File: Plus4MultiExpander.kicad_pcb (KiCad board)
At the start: 2 copper layers, 62.2 x 99.9 mm, 11 parts, among them CN1 EDGE_CONN, CN2 C16_NEWSTYLE_EXP_PORT_1, CN3 C16_NEWSTYLE_EXP_PORT_2, CN4 C16_NEWSTYLE_EXP_PORT_3, U1 74LS245, U2 74LS245

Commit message: More honing
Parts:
- moved D1 0.25 mm to (136.5, 134.5)
- moved D2 0.25 mm to (140.8, 134.5)
- moved R1 0.25 mm to (132.2, 134.5)

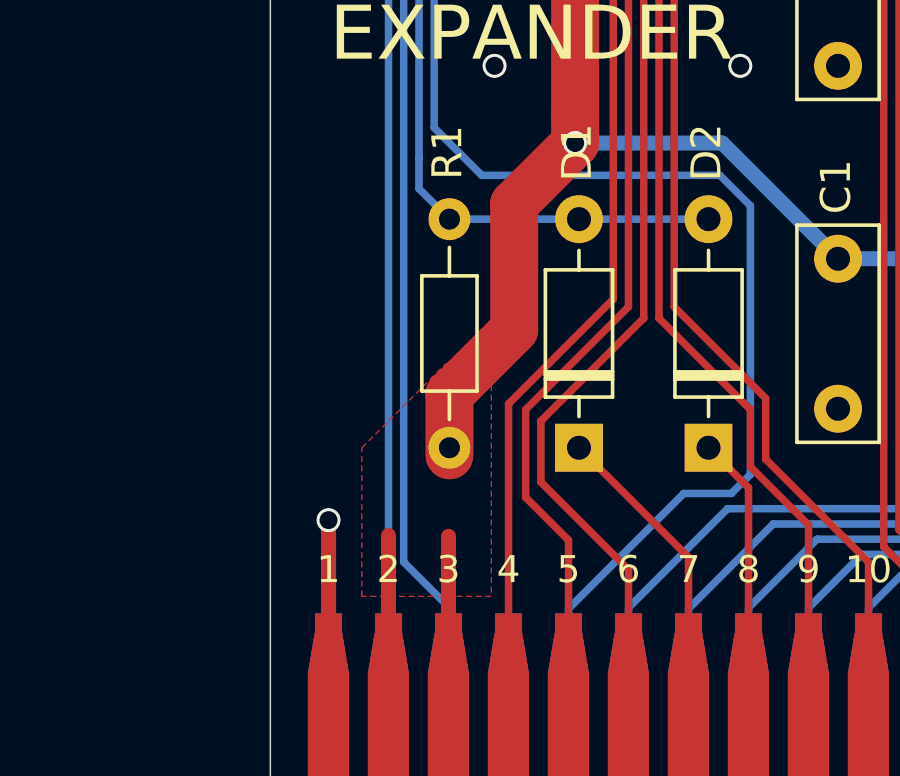
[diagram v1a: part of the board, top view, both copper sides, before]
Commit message: Add 3D model of connector
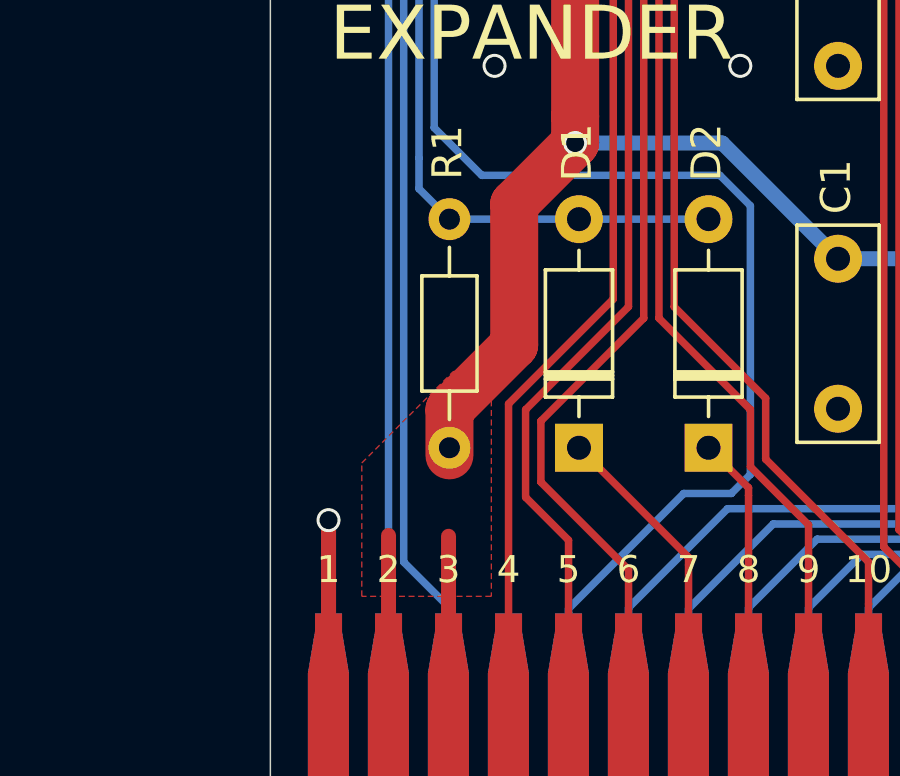
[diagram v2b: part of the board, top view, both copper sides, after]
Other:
- board text added: "INSPIRED BY WORK FROM SOLDER/SYNERGY"

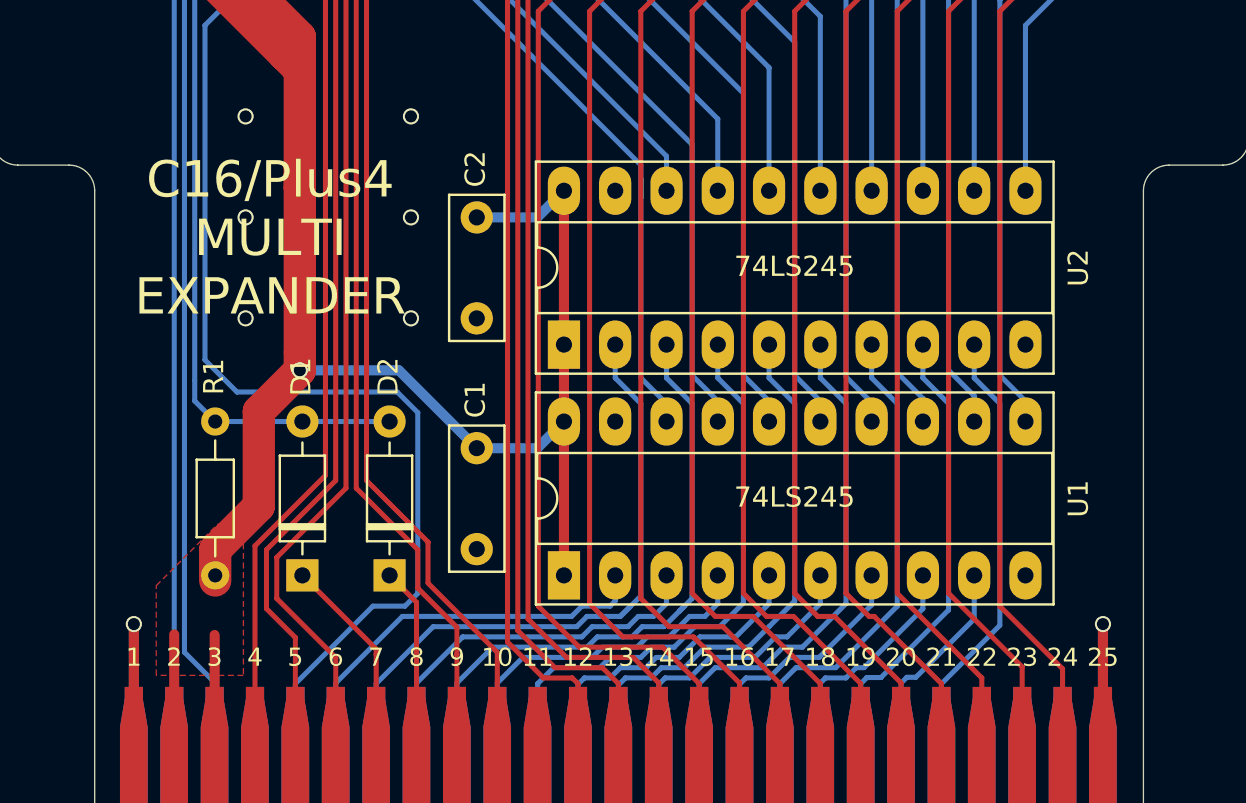
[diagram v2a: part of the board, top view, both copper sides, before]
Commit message: Tidy up silkscreen
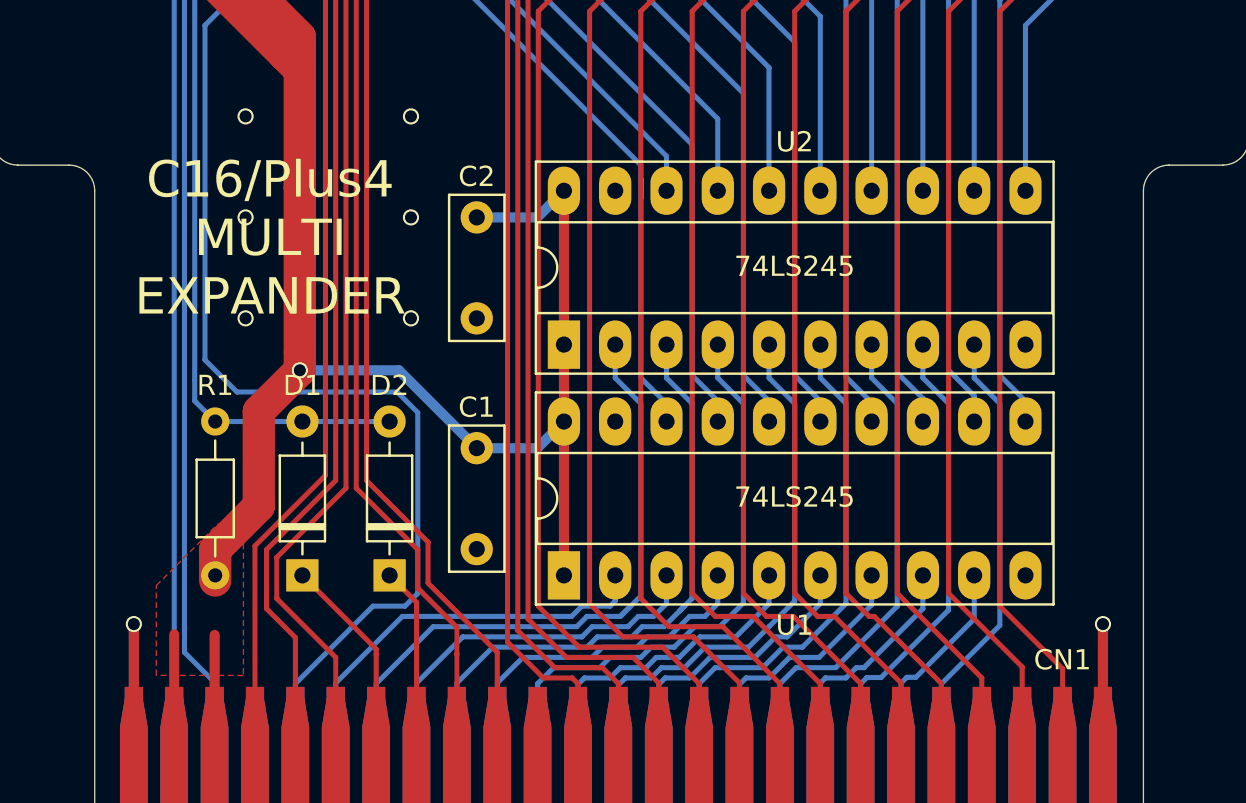
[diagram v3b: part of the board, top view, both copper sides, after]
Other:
- board text removed: "1"
- board text removed: "10"
- board text removed: "11"
- board text removed: "12"
- board text removed: "13"
- board text removed: "14"
- board text removed: "15"
- board text removed: "16"
- board text removed: "17"
- board text removed: "18"
- board text removed: "19"
- board text removed: "2"
- board text removed: "20"
- board text removed: "21"
- board text removed: "22"
- board text removed: "23"
- board text removed: "24"
- board text removed: "25"
- board text removed: "3"
- board text removed: "4"
- board text removed: "5"
- board text removed: "6"
- board text removed: "7"
- board text removed: "8"
- board text removed: "9"
- board text removed: "A"
- board text removed: "AA"
- board text removed: "B"
- board text removed: "BB"
- board text removed: "C"
- board text removed: "CC"
- board text removed: "D"
- board text removed: "E"
- board text removed: "F"
- board text removed: "H"
- board text removed: "J"
- board text removed: "K"
- board text removed: "L"
- board text removed: "M"
- board text removed: "N"
- board text removed: "P"
- board text removed: "R"
- board text removed: "S"
- board text removed: "T"
- board text removed: "U"
- board text removed: "V"
- board text removed: "W"
- board text removed: "X"
- board text removed: "Y"
- board text removed: "Z"

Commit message: Add credits and license
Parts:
- added C3: 220u, Capacitor_THT:CP_Radial_D8.0mm_P3.50mm, F.Cu at (128.1, 85.9)
- added V0: LICENSE, Plus4MultiExpander:cc_by_nc_sa, B.Cu at (135.9, 119.3)
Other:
- board text added: "CC-BY-NC-SA © SukkoPera 2023 Inspired by work from Solder/Synergy github.com/SukkoPera/Plus4MultiExpander"
- board text removed: "INSPIRED BY WORK FROM SOLDER/SYNERGY"

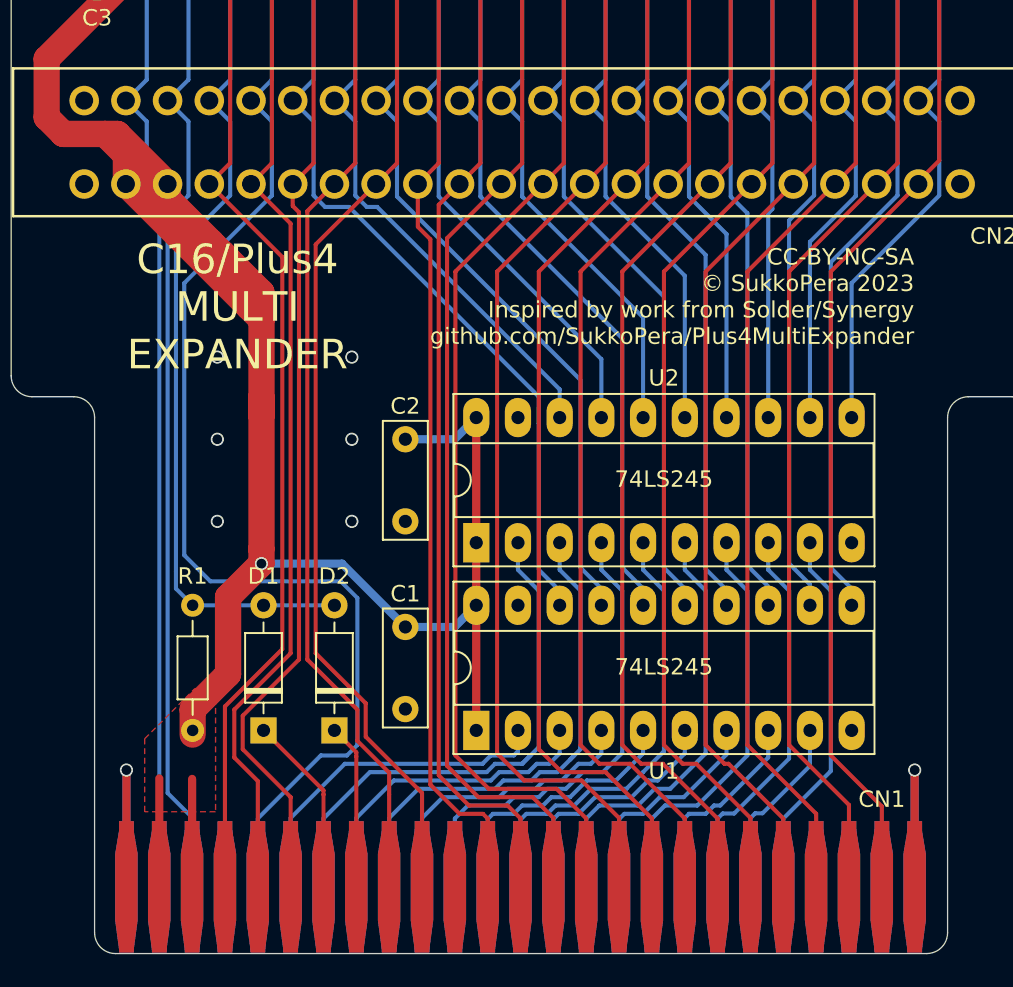
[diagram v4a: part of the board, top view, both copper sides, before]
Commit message: Generate /C2 with NAND gate
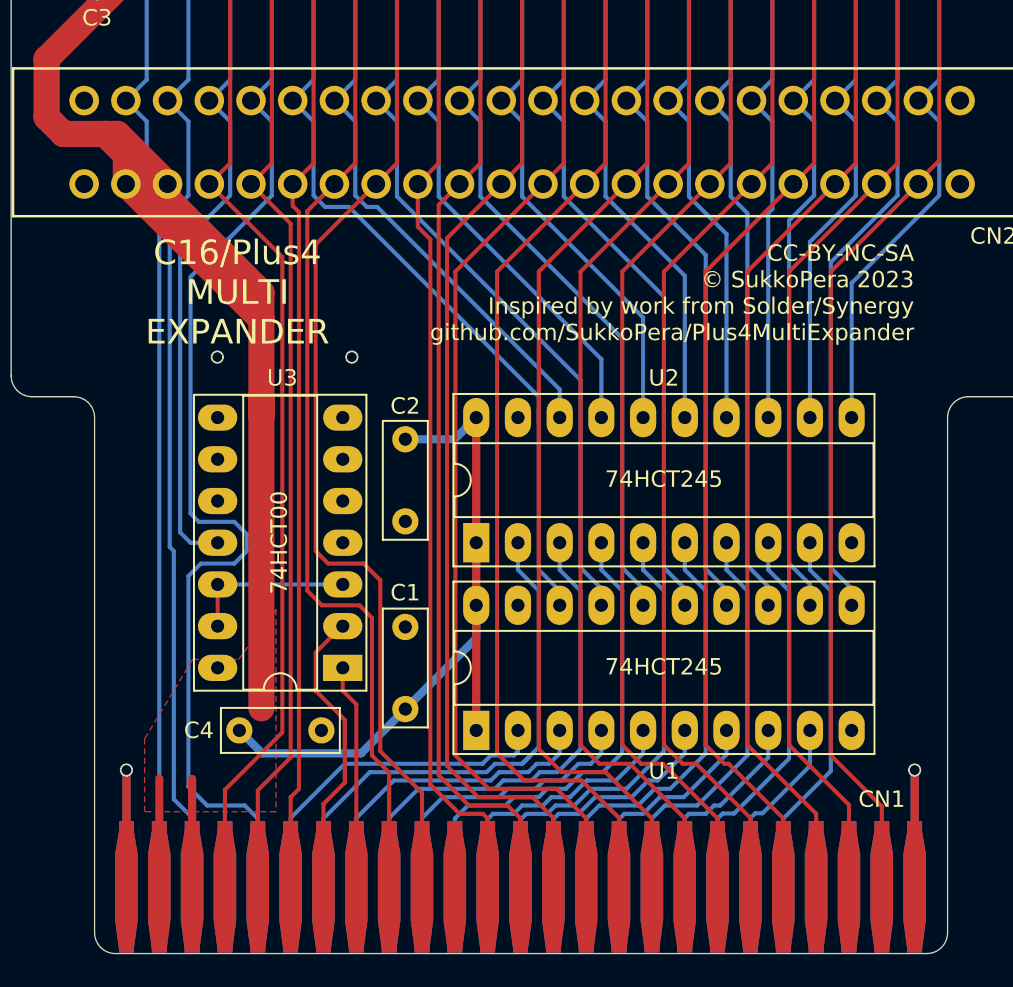
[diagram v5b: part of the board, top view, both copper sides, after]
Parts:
- removed D1, D2: 1n4148, Diode_THT:D_DO-35_SOD27_P7.62mm_Horizontal
- removed R1: 4.7k, Resistor_THT:R_Axial_DIN0204_L3.6mm_D1.6mm_P7.62mm_Horizontal
- added C4: 100n, Capacitor_THT:C_Disc_D7.0mm_W2.5mm_P5.00mm, F.Cu at (135.1, 134.5)
- added U3: 74HCT00, Package_DIP:DIP-14_W7.62mm_Socket_LongPads, F.Cu at (141.4, 130.7)
- U1, U2: value 74LS245 -> 74HCT245
- moved V0 19.1 mm to (152.3, 109.5)
- moved C1 5.00 mm to (145.2, 133.2), turned to 90 degrees
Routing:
- net /~c2: track 89.8 -> 78.7 mm
- net Net-(U3-Pad12): track 0.00 -> 10.2 mm
- net /~c2lo: track 11.0 -> 17.9 mm
- net /phi0: track 115.2 -> 111.0 mm
- net /~c2hi: track 10.1 -> 13.9 mm
- net /~c1hi: track 93.7 -> 91.2 mm
- net +5V: track 241.0 -> 242.4 mm, vias 1 -> 0
- net /~cs1: track 93.6 -> 95.0 mm
- net /~cs0: track 95.1 -> 96.4 mm
- net /r_~w: track 93.9 -> 92.7 mm
- net GND: vias 8 -> 4

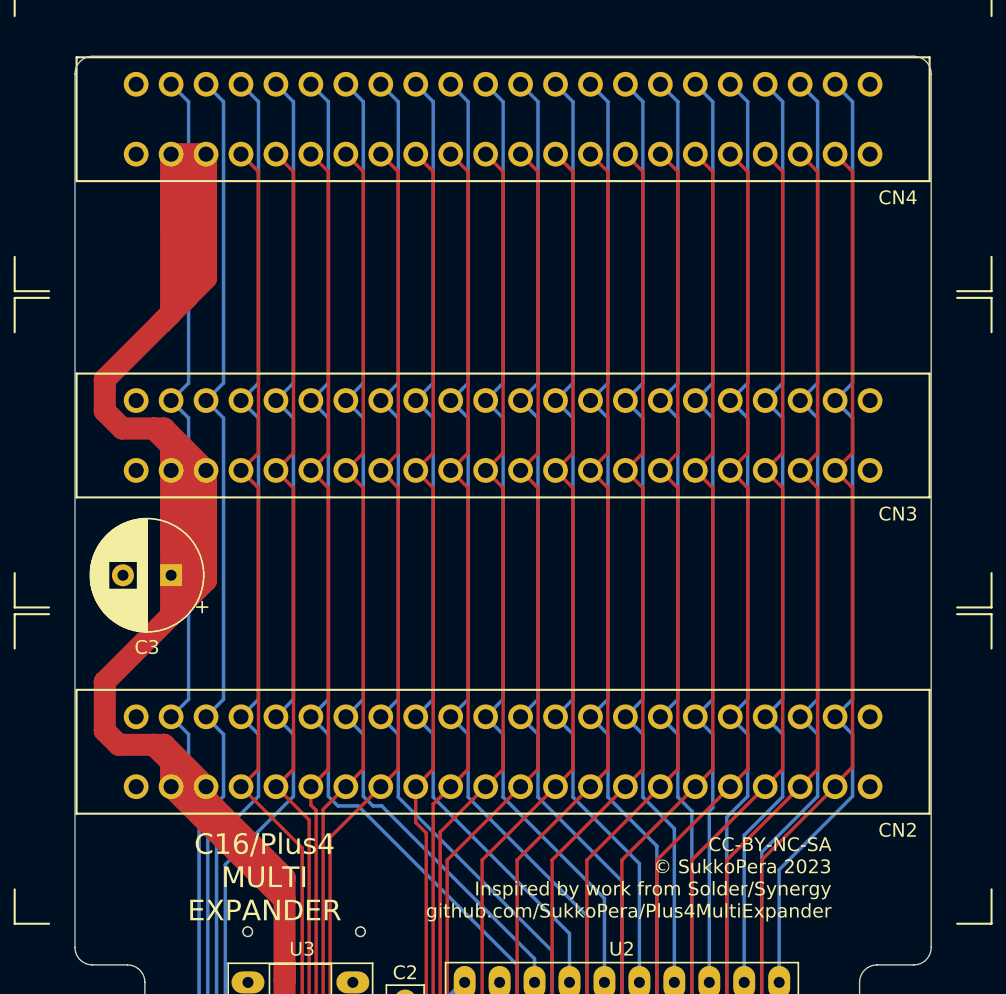
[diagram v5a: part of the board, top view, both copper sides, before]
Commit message: Add standoff holes
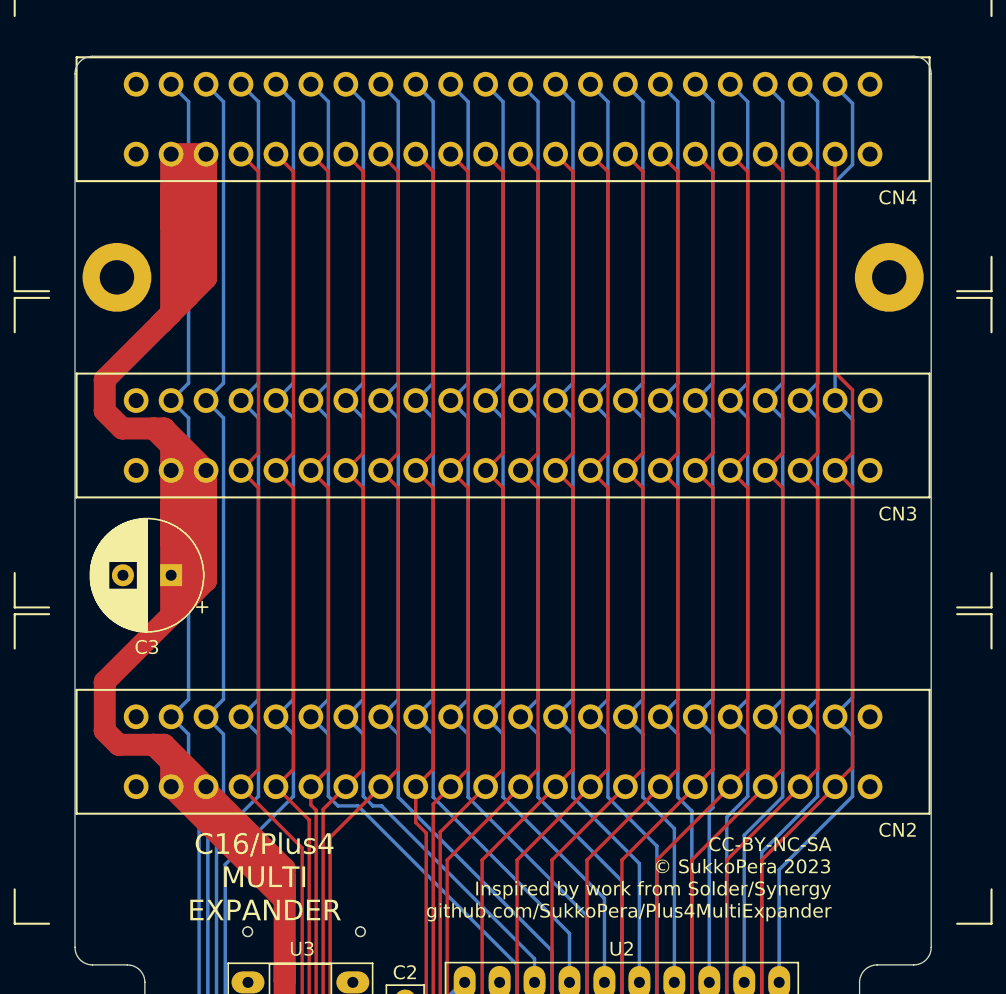
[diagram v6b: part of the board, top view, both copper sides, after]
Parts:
- added H1: HOLE_STANDOFF, MountingHole:MountingHole_2.5mm_Pad, F.Cu at (124.2, 63.1)
- added H2: HOLE_STANDOFF, MountingHole:MountingHole_2.5mm_Pad, F.Cu at (180.3, 64.2)
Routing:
- net +5V: track 242.4 -> 254.0 mm
